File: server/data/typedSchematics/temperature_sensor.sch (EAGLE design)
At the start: 1 part, among them U1 MCP9808

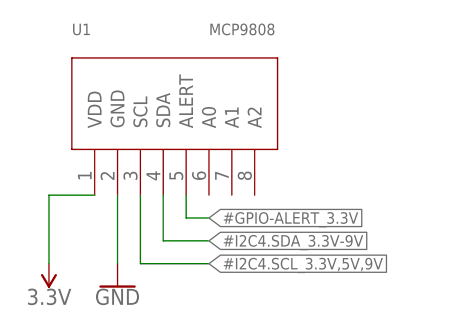
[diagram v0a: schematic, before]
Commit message: Redefining typed annotation
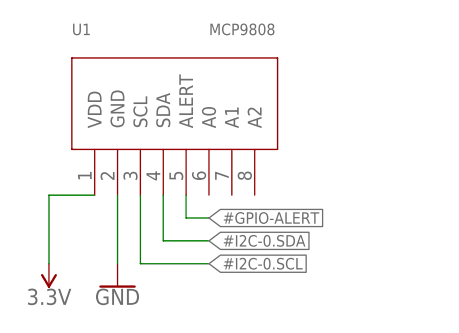
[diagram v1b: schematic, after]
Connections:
- net #GPIO-ALERT_3.3V renamed #GPIO-ALERT
- net #I2C4.SCL_3.3V,5V,9V renamed #I2C-0.SCL
- net #I2C4.SDA_3.3V-9V renamed #I2C-0.SDA
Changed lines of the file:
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@@
 </segment>
 </net>
-<net name="#I2C4.SCL_3.3V,5V,9V" class="0">
+<net name="#I2C-0.SCL" class="0">
 <segment>
 <pinref part="U1" gate="G$1" pin="SCL"/>
@@
 </segment>
 </net>
-<net name="#I2C4.SDA_3.3V-9V" class="0">
+<net name="#I2C-0.SDA" class="0">
 <segment>
 <pinref part="U1" gate="G$1" pin="SDA"/>
@@
 </segment>
 </net>
-<net name="#GPIO-ALERT_3.3V" class="0">
+<net name="#GPIO-ALERT" class="0">
 <segment>
 <pinref part="U1" gate="G$1" pin="ALERT"/>

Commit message: Add typed power
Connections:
- net 3.3V renamed @VIN_3.3V
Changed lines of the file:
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@@
 <parts>
 <part name="GND1" library="SparkFun-PowerSymbols" library_urn="urn:adsk.eagle:library:530" deviceset="GND" device=""/>
-<part name="SUPPLY4" library="SparkFun-PowerSymbols" library_urn="urn:adsk.eagle:library:530" deviceset="3.3V" device=""/>
 <part name="U1" library="MCP9808" deviceset="MCP9808" device=""/>
 </parts>
@@
 <instance part="GND1" gate="1" x="-5.08" y="-20.32" smashed="yes">
 <attribute name="VALUE" x="-5.08" y="-20.574" size="1.778" layer="96" align="top-center"/>
-</instance>
-<instance part="SUPPLY4" gate="G$1" x="-12.7" y="-17.78" smashed="yes" rot="R180">
-<attribute name="VALUE" x="-12.7" y="-20.574" size="1.778" layer="96" rot="R180" align="bottom-center"/>
 </instance>
 <instance part="U1" gate="G$1" x="0" y="0" smashed="yes">
@@
 <pinref part="GND1" gate="1" pin="GND"/>
 <wire x1="-5.08" y1="-10.16" x2="-5.08" y2="-17.78" width="0.1524" layer="91"/>
-</segment>
-</net>
-<net name="3.3V" class="0">
-<segment>
-<pinref part="SUPPLY4" gate="G$1" pin="3.3V"/>
-<wire x1="-12.7" y1="-17.78" x2="-12.7" y2="-10.16" width="0.1524" layer="91"/>
-<pinref part="U1" gate="G$1" pin="VDD"/>
-<wire x1="-12.7" y1="-10.16" x2="-7.62" y2="-10.16" width="0.1524" layer="91"/>
 </segment>
 </net>
@@
 </segment>
 </net>
+<net name="@VIN_3.3V" class="0">
+<segment>
+<wire x1="-12.7" y1="-17.78" x2="-12.7" y2="-10.16" width="0.1524" layer="91"/>
+<pinref part="U1" gate="G$1" pin="VDD"/>
+<wire x1="-12.7" y1="-10.16" x2="-7.62" y2="-10.16" width="0.1524" layer="91"/>
+<label x="-12.7" y="-17.78" size="1.27" layer="95" rot="R180" xref="yes"/>
+</segment>
+</net>

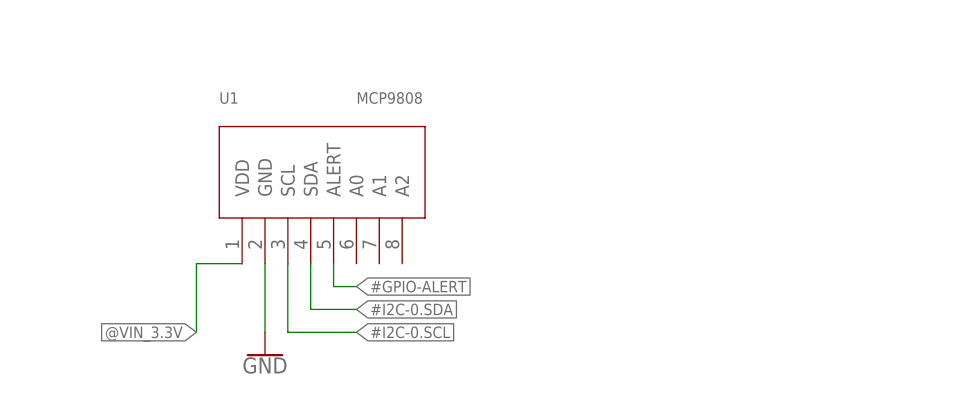
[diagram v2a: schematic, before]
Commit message: Adding I2C options in schematic + Voltage fix
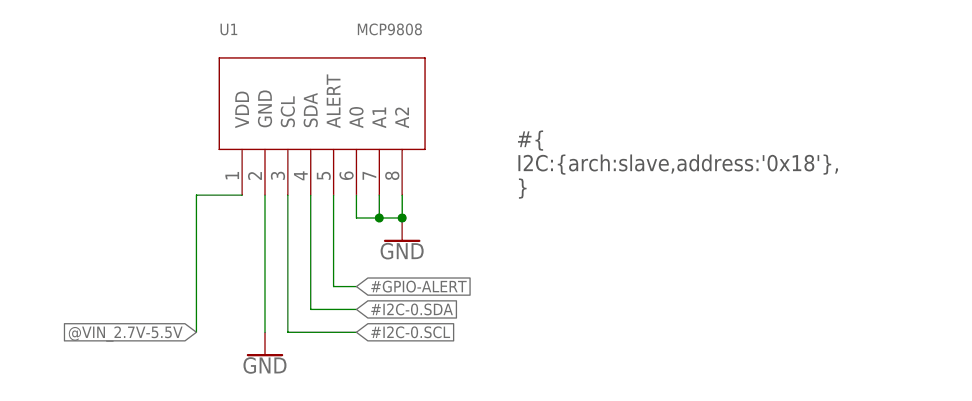
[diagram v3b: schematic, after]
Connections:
- net @VIN_3.3V renamed @VIN_2.7V-5.5V
- net GND: now also U1.A0, U1.A1, U1.A2
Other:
- note added: "#{ I2C:{arch:slave,address:'0x18'}, }"
- moved on the sheet: U1
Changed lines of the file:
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@@
 <part name="GND1" library="SparkFun-PowerSymbols" library_urn="urn:adsk.eagle:library:530" deviceset="GND" device=""/>
 <part name="U1" library="MCP9808" deviceset="MCP9808" device=""/>
+<part name="GND2" library="SparkFun-PowerSymbols" library_urn="urn:adsk.eagle:library:530" deviceset="GND" device=""/>
 </parts>
 <sheets>
 <sheet>
 <plain>
+<text x="22.86" y="-2.54" size="1.778" layer="97">#{
+I2C:{arch:slave,address:'0x18'},
+}</text>
 </plain>
 <instances>
@@
 <attribute name="VALUE" x="-5.08" y="-20.574" size="1.778" layer="96" align="top-center"/>
 </instance>
-<instance part="U1" gate="G$1" x="0" y="0" smashed="yes">
-<attribute name="NAME" x="-10.16" y="7.62" size="1.27" layer="95"/>
-<attribute name="VALUE" x="5.08" y="7.62" size="1.27" layer="95"/>
+<instance part="U1" gate="G$1" x="0" y="7.62" smashed="yes">
+<attribute name="NAME" x="-10.16" y="15.24" size="1.27" layer="95"/>
+<attribute name="VALUE" x="5.08" y="15.24" size="1.27" layer="95"/>
+</instance>
+<instance part="GND2" gate="1" x="10.16" y="-7.62" smashed="yes">
+<attribute name="VALUE" x="10.16" y="-7.874" size="1.778" layer="96" align="top-center"/>
 </instance>
 </instances>
@@
 <pinref part="U1" gate="G$1" pin="GND"/>
 <pinref part="GND1" gate="1" pin="GND"/>
-<wire x1="-5.08" y1="-10.16" x2="-5.08" y2="-17.78" width="0.1524" layer="91"/>
+<wire x1="-5.08" y1="-2.54" x2="-5.08" y2="-17.78" width="0.1524" layer="91"/>
+</segment>
+<segment>
+<pinref part="U1" gate="G$1" pin="A0"/>
+<pinref part="GND2" gate="1" pin="GND"/>
+<wire x1="5.08" y1="-2.54" x2="5.08" y2="-5.08" width="0.1524" layer="91"/>
+<wire x1="5.08" y1="-5.08" x2="7.62" y2="-5.08" width="0.1524" layer="91"/>
+<pinref part="U1" gate="G$1" pin="A1"/>
+<wire x1="7.62" y1="-5.08" x2="10.16" y2="-5.08" width="0.1524" layer="91"/>
+<wire x1="7.62" y1="-2.54" x2="7.62" y2="-5.08" width="0.1524" layer="91"/>
+<junction x="7.62" y="-5.08"/>
+<pinref part="U1" gate="G$1" pin="A2"/>
+<wire x1="10.16" y1="-2.54" x2="10.16" y2="-5.08" width="0.1524" layer="91"/>
+<junction x="10.16" y="-5.08"/>
 </segment>
 </net>
@@
 <segment>
 <pinref part="U1" gate="G$1" pin="SCL"/>
-<wire x1="-2.54" y1="-10.16" x2="-2.54" y2="-17.78" width="0.1524" layer="91"/>
+<wire x1="-2.54" y1="-2.54" x2="-2.54" y2="-17.78" width="0.1524" layer="91"/>
 <wire x1="-2.54" y1="-17.78" x2="5.08" y2="-17.78" width="0.1524" layer="91"/>
 <label x="5.08" y="-17.78" size="1.27" layer="95" xref="yes"/>
@@
 <segment>
 <pinref part="U1" gate="G$1" pin="SDA"/>
-<wire x1="0" y1="-10.16" x2="0" y2="-15.24" width="0.1524" layer="91"/>
+<wire x1="0" y1="-2.54" x2="0" y2="-15.24" width="0.1524" layer="91"/>
 <wire x1="0" y1="-15.24" x2="5.08" y2="-15.24" width="0.1524" layer="91"/>
 <label x="5.08" y="-15.24" size="1.27" layer="95" xref="yes"/>
@@
 <segment>
 <pinref part="U1" gate="G$1" pin="ALERT"/>
-<wire x1="2.54" y1="-10.16" x2="2.54" y2="-12.7" width="0.1524" layer="91"/>
+<wire x1="2.54" y1="-2.54" x2="2.54" y2="-12.7" width="0.1524" layer="91"/>
 <wire x1="2.54" y1="-12.7" x2="5.08" y2="-12.7" width="0.1524" layer="91"/>
 <label x="5.08" y="-12.7" size="1.27" layer="95" xref="yes"/>
 </segment>
 </net>
-<net name="@VIN_3.3V" class="0">
+<net name="@VIN_2.7V-5.5V" class="0">
 <segment>
-<wire x1="-12.7" y1="-17.78" x2="-12.7" y2="-10.16" width="0.1524" layer="91"/>
+<wire x1="-12.7" y1="-17.78" x2="-12.7" y2="-2.54" width="0.1524" layer="91"/>
 <pinref part="U1" gate="G$1" pin="VDD"/>
-<wire x1="-12.7" y1="-10.16" x2="-7.62" y2="-10.16" width="0.1524" layer="91"/>
+<wire x1="-12.7" y1="-2.54" x2="-7.62" y2="-2.54" width="0.1524" layer="91"/>
 <label x="-12.7" y="-17.78" size="1.27" layer="95" rot="R180" xref="yes"/>
 </segment>
@@
 </drawing>
 <compatibility>
+<note version="6.3" minversion="6.2.2" severity="warning">
+Since Version 6.2.2 text objects can contain more than one line,
+which will not be processed correctly with this version.
+</note>
 <note version="8.2" severity="warning">
 Since Version 8.2, EAGLE supports online libraries. The ids

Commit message: Schematics with require annotation
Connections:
- net #GPIO-ALERT renamed #GPIO-ALERT!
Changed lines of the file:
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@@
 </segment>
 </net>
-<net name="#GPIO-ALERT" class="0">
+<net name="#GPIO-ALERT!" class="0">
 <segment>
 <pinref part="U1" gate="G$1" pin="ALERT"/>
